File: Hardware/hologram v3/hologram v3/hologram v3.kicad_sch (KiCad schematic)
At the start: 700 parts, among them J1 USB_C_Receptacle_USB2.0_16P, J2 Conn_01x06_Socket, SW1 SW_Reset, SW2 SW_Boot, SW3 SW_opt1, SW4 SW_opt2, U1 SM16106SC, U10 SM16106SC, U11 SM16106SC, U12 SM16106SC, U13 SM16106SC, U14 SM16106SC, U15 SM16106SC, U16 SM16106SC, U17 SM16106SC, U18 SM16106SC, U19 SM16106SC, U2 SM16106SC, U20 SM16106SC, U21 SM16106SC, U22 SM16106SC, U23 SM16106SC, U24 SM16106SC, U25 SM16106SC, U26 SM16106SC, U27 SM16106SC, U28 SM16106SC, U29 SM16106SC, U3 SM16106SC, U30 SM16106SC, U31 SM16106SC, U32 SM16106SC, U33 ESP32-S3-WROOM-1(N16R8), U34 SY8286ARAC 12v->4v, U36 SY8286ARAC 12v->3.3v, U4 SM16106SC, U5 SM16106SC, U6 SM16106SC, U7 SM16106SC, U8 SM16106SC, U9 SM16106SC

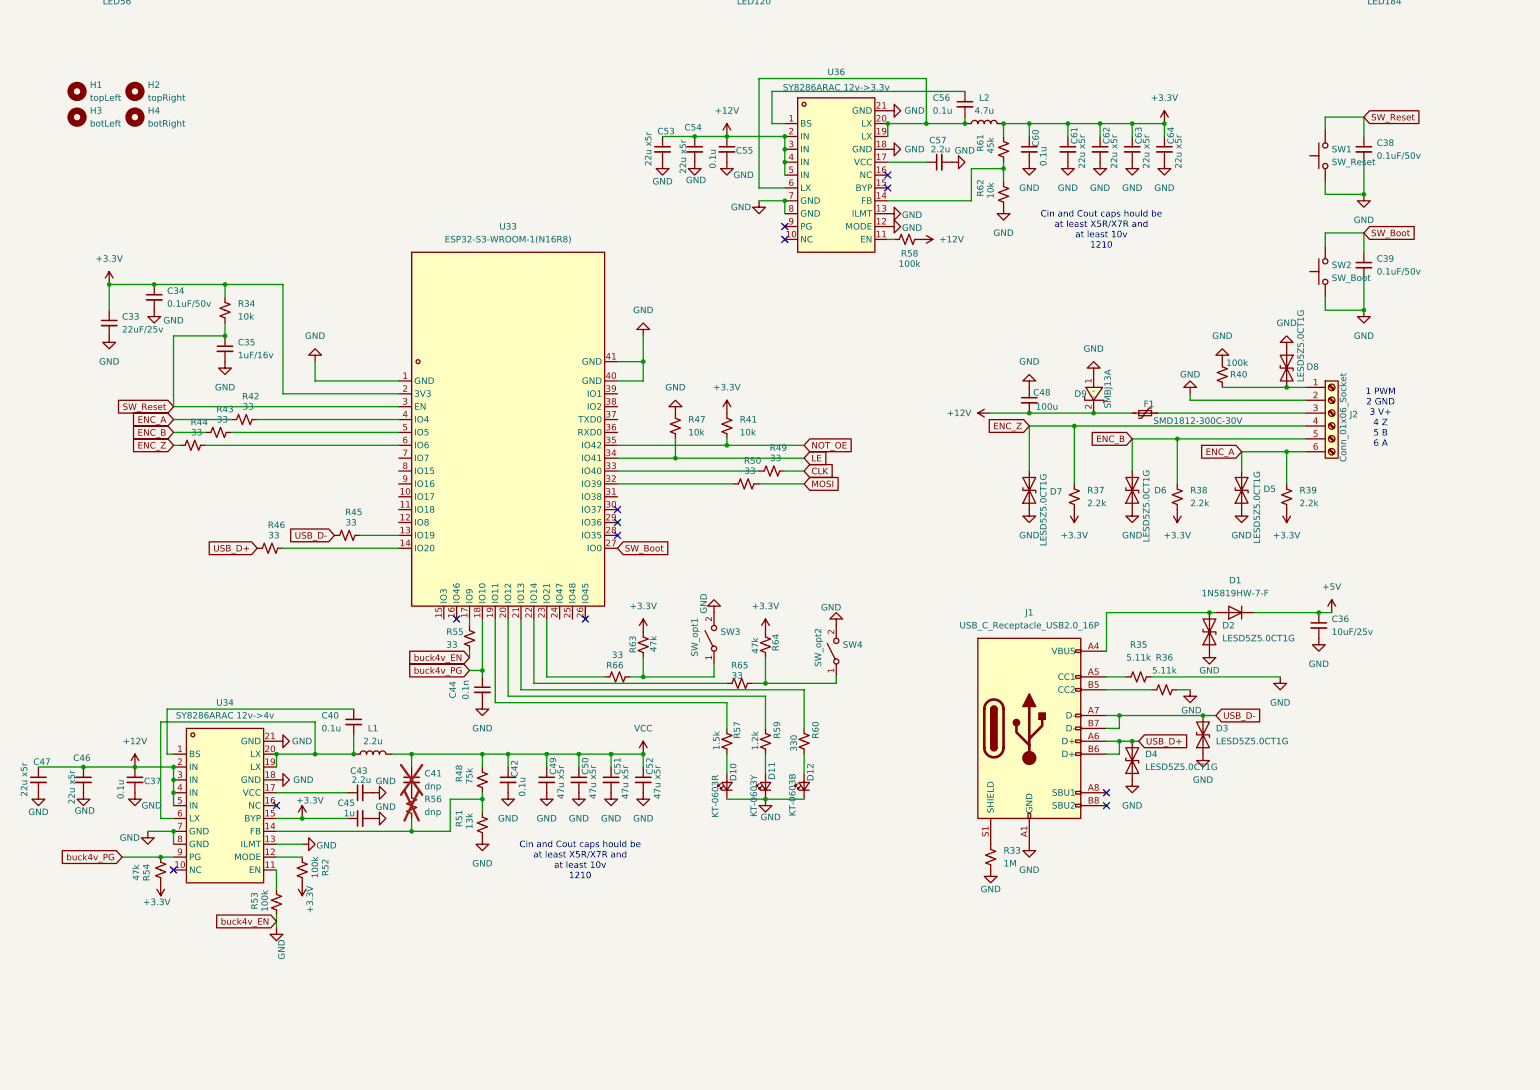
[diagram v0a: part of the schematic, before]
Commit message: kicad placed all parts, just need to wire 3.3v buck then review design
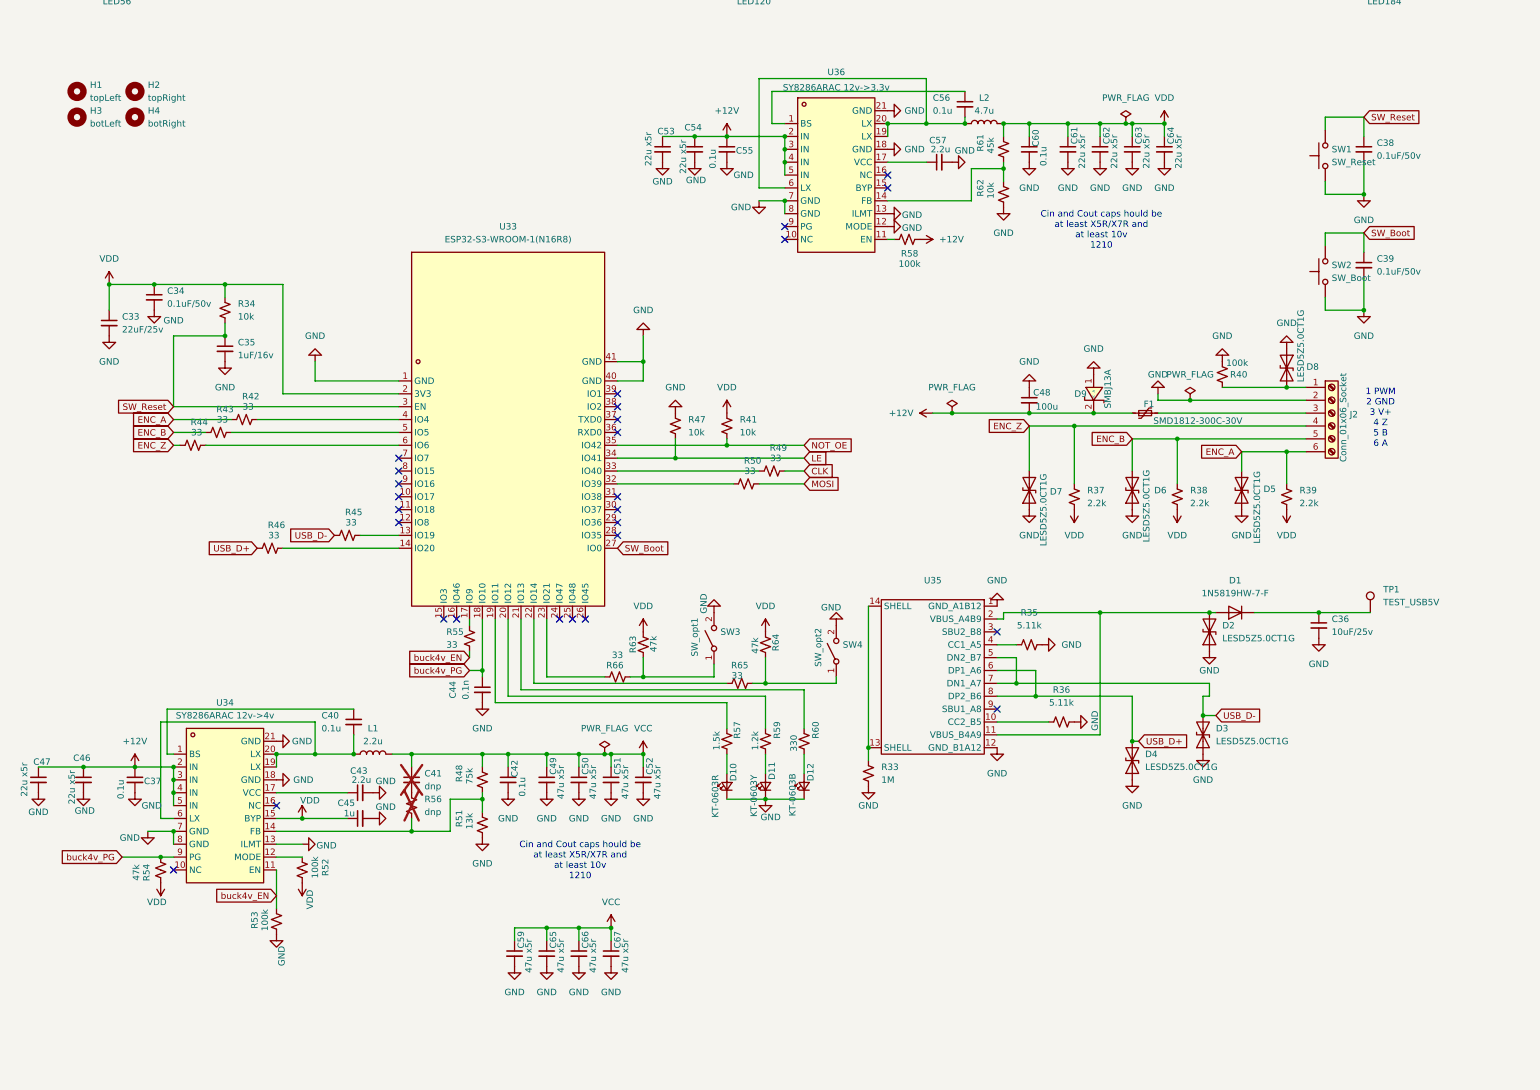
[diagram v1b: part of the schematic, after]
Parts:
- removed J1: USB_C_Receptacle_USB2.0_16P, easyeda:USB-C-SMD_TYPE-C-6PIN-2MD-073, symbol Connector:USB_C_Receptacle_USB2.0_16P
- added C59, C65, C66, C67: 47u x5r, Capacitor_SMD:C_1210_3225Metric, symbol Device:C_Small
- added TP1: TEST_USB5V, TestPoint:TestPoint_Pad_3.0x3.0mm, symbol Connector:TestPoint
- added U35: ~, easyeda:USB-C-SMD_TYPE-C-6PIN-2MD-073, symbol easyeda:Type-c_16pin_2md(073)
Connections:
- net +3.3V is gone; now on net VDD: C33.1, C34.1, C45.1, C60.1, C61.1, C62.1, C63.1, C64.1, L2.2, R34.1, R37.2, R38.2, R39.2, R41.1, R52.1, R54.1, R61.1, R63.2, R64.1, U33.2 (3V3), U34.15 (BYP)
- net GND: now also C59.2, C65.2, C66.2, C67.2, U35.1 (GND_A1B12), U35.12 (GND_B1A12); no longer R55.2
- net USB_D+: now also U35.6 (DP1_A6), U35.8 (DP2_B6)
- net USB_D-: now also U35.5 (DN2_B7), U35.7 (DN1_A7)
- net VCC: now also C59.1, C65.1, C66.1, C67.1
- net at R35.1: now also U35.4 (CC1_A5)
- net at D1.2 (A), D2.2 (A2): now also U35.11 (VBUS_B4A9), U35.2 (VBUS_A4B9)
- net at R36.1: now also U35.10 (CC2_B5)
- net at R33.1: now also U35.13 (SHELL), U35.14 (SHELL)
- net buck4v_EN: now reaches R53.1, U34.11 (EN)
- net buck4v_EN: now also R55.2
- net +5V: no longer names the net of C36.1, D1.1 (K)
- net +5V: now also TP1.1
- no-connect marks 14 -> 28
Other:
- moved on the sheet: R33, R35, R36, R53

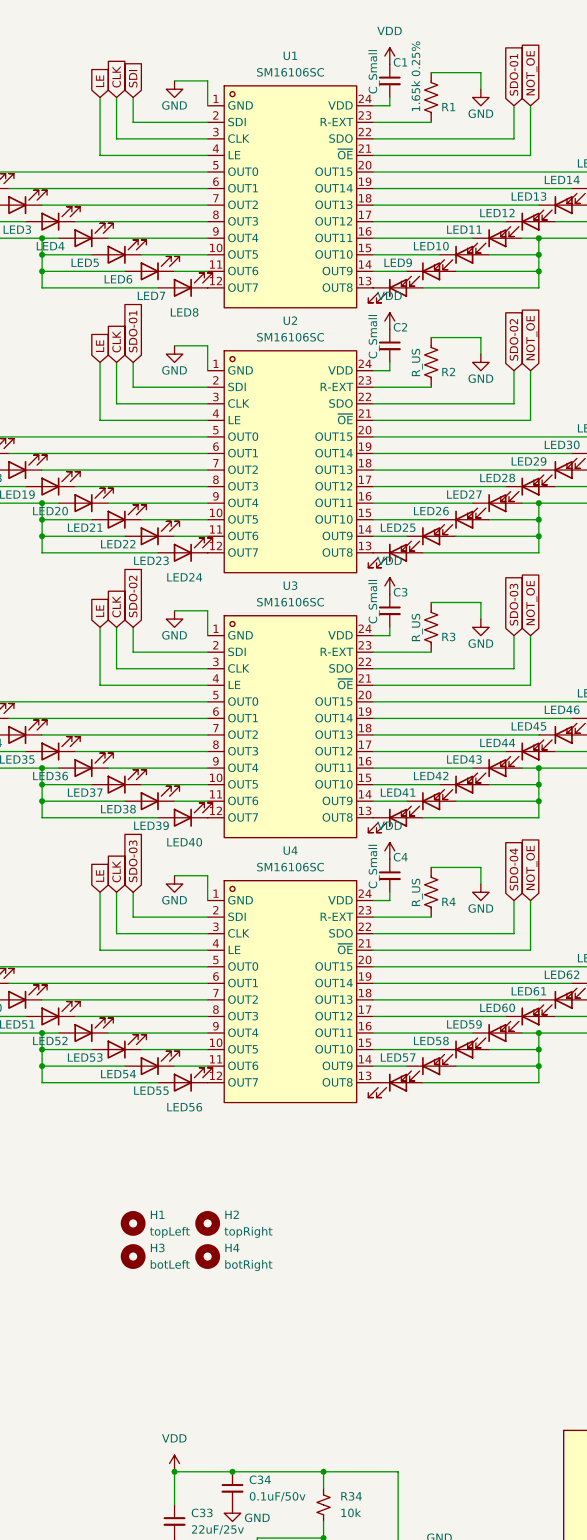
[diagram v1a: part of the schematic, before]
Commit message: kicad routed le, oe, clk, mosi, addded debug header pins
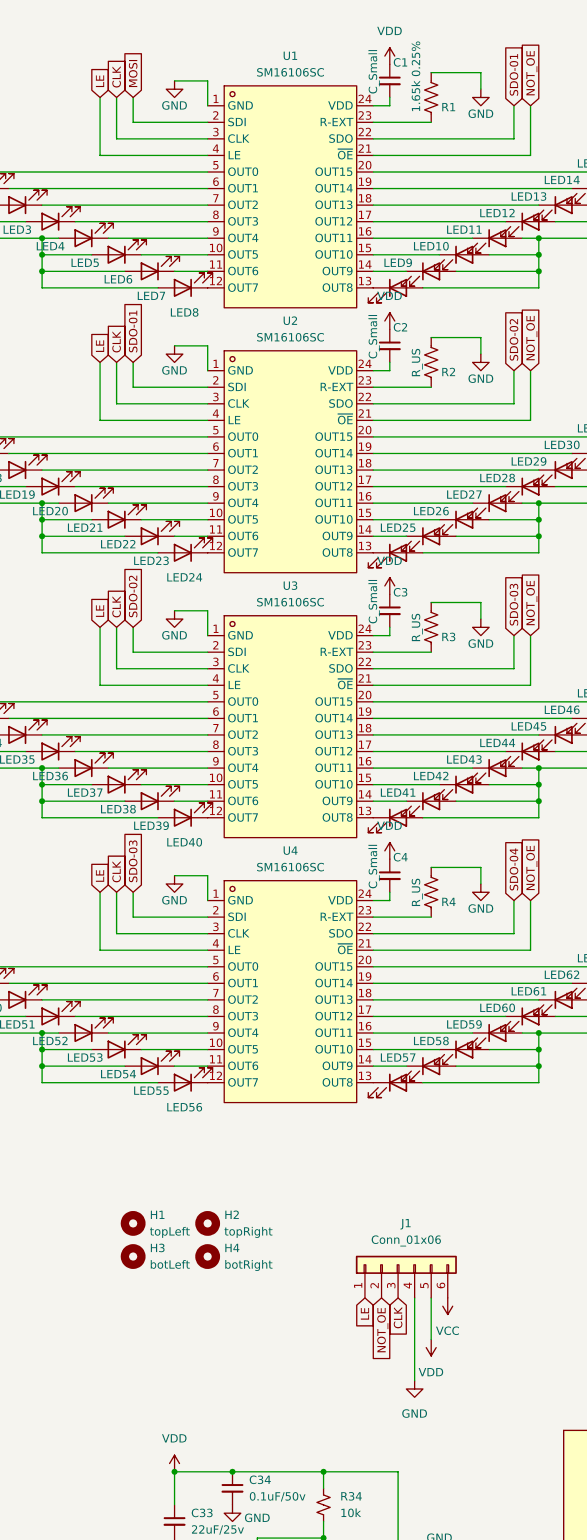
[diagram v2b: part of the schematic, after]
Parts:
- added J1: Conn_01x06, Connector_PinHeader_2.54mm:PinHeader_1x06_P2.54mm_Vertical, symbol Connector_Generic:Conn_01x06
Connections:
- net SDI is gone; now on net MOSI: U1.2 (SDI)
- net CLK: now also J1.3 (Pin_3)
- net GND: now also J1.4 (Pin_4)
- net LE: now also J1.1 (Pin_1)
- net NOT_OE: now also J1.2 (Pin_2)
- net VCC: now also J1.6 (Pin_6)
- net VDD: now also J1.5 (Pin_5)

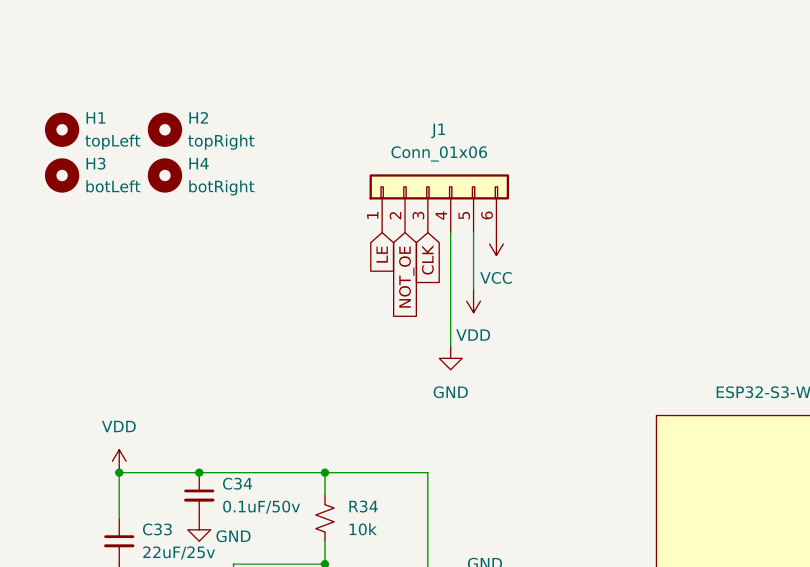
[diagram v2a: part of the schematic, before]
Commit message: wired in the debug pins
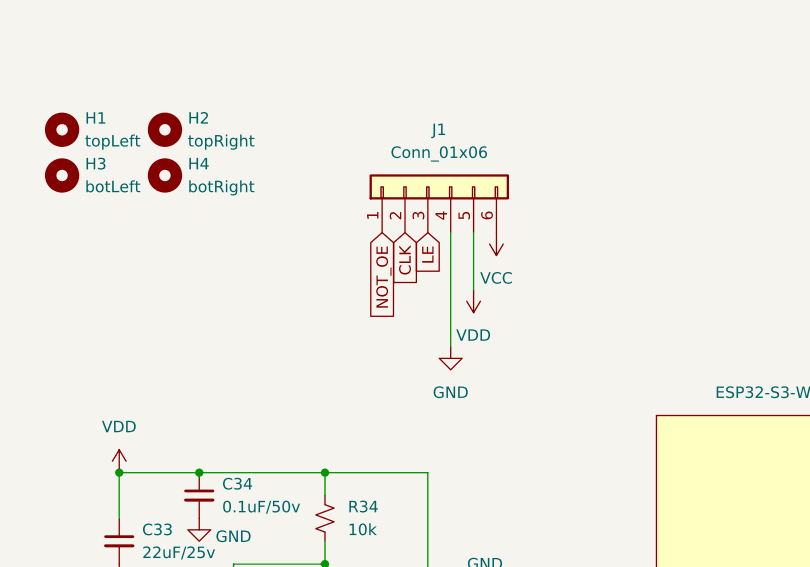
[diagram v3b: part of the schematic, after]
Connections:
- net CLK: now also J1.2 (Pin_2); no longer J1.3 (Pin_3)
- net LE: now also J1.3 (Pin_3); no longer J1.1 (Pin_1)
- net NOT_OE: now also J1.1 (Pin_1); no longer J1.2 (Pin_2)
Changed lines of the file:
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@@
 		)
 	)
-	(global_label "CLK"
-		(shape input)
-		(at 54.61 25.4 270)
-		(fields_autoplaced yes)
-		(effects
-			(font
-				(size 1.27 1.27)
-			)
-			(justify right)
-		)
-		(property "Intersheetrefs" "${INTERSHEET_REFS}"
-			(at 54.61 31.9533 90)
-			(effects
-				(font
-					(size 1.27 1.27)
-				)
-				(justify right)
-				(hide yes)
-			)
-		)
-	)
 	(global_label "buck4v_PG"
 		(shape input)
@@
 		)
 	)
-	(global_label "NOT_OE"
-		(shape input)
-		(at 52.07 25.4 270)
-		(fields_autoplaced yes)
-		(effects
-			(font
-				(size 1.27 1.27)
-			)
-			(justify right)
-		)
-		(property "Intersheetrefs" "${INTERSHEET_REFS}"
-			(at 52.07 35.4609 90)
-			(effects
-				(font
-					(size 1.27 1.27)
-				)
-				(justify right)
-				(hide yes)
-			)
-		)
-	)
 	(global_label "CLK"
 		(shape input)
@@
 		)
 	)
+	(global_label "NOT_OE"
+		(shape input)
+		(at 49.53 25.4 270)
+		(fields_autoplaced yes)
+		(effects
+			(font
+				(size 1.27 1.27)
+			)
+			(justify right)
+		)
+		(property "Intersheetrefs" "${INTERSHEET_REFS}"
+			(at 49.53 35.4609 90)
+			(effects
+				(font
+					(size 1.27 1.27)
+				)
+				(justify right)
+				(hide yes)
+			)
+		)
+	)
 	(global_label "SDO-12"
 		(shape input)
@@
 		)
 	)
+	(global_label "LE"
+		(shape input)
+		(at 54.61 25.4 270)
+		(fields_autoplaced yes)
+		(effects
+			(font
+				(size 1.27 1.27)
+			)
+			(justify right)
+		)
+		(property "Intersheetrefs" "${INTERSHEET_REFS}"
+			(at 54.61 30.5623 90)
+			(effects
+				(font
+					(size 1.27 1.27)
+				)
+				(justify right)
+				(hide yes)
+			)
+		)
+	)
 	(global_label "CLK"
 		(shape input)
@@
 	(global_label "CLK"
 		(shape input)
+		(at 52.07 25.4 270)
+		(fields_autoplaced yes)
+		(effects
+			(font
+				(size 1.27 1.27)
+			)
+			(justify right)
+		)
+		(property "Intersheetrefs" "${INTERSHEET_REFS}"
+			(at 52.07 31.9533 90)
+			(effects
+				(font
+					(size 1.27 1.27)
+				)
+				(justify right)
+				(hide yes)
+			)
+		)
+	)
+	(global_label "CLK"
+		(shape input)
 		(at 157.48 88.9 0)
 		(fields_autoplaced yes)
@@
 				(hide yes)
 			)
-		)
-	)
-	(global_label "LE"
-		(shape input)
-		(at 49.53 25.4 270)
-		(fields_autoplaced yes)
-		(effects
-			(font
-				(size 1.27 1.27)
-			)
-			(justify right)
-		)
-		(property "Intersheetrefs" "${INTERSHEET_REFS}"
-			(at 49.53 30.5623 90)
-			(effects
-				(font
-					(size 1.27 1.27)
-				)
-				(justify right)
-				(hide yes)
-			)

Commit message: hologram done and submitted for printing
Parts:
- C33: value 22uF/25v -> 22u
- C34, C38, C39: value 0.1uF/50v -> 0.1u
- C35: value 1uF/16v -> 1u
- C36: value 10uF/25v -> 10u
- C44: value 0.1n -> 0.1u
- C46, C47, C53, C54, C61, C62, C63, C64: value 22u x5r -> 22u
- C48: symbol Device:C_Small -> Device:C_Polarized_US; LCSC Part (none) -> C46550465
- C49, C50, C51, C52, C59, C65, C66, C67: value 47u x5r -> 47u
- D5, D6, D7, D8: symbol Device:D_TVS -> easyeda:LESD5Z5.0CT1G; LCSC Part (none) -> C136167
- D9: LCSC Part C10209 -> C151252
- F1: LCSC Part (none) -> C47002391
- J2: footprint TerminalBlock:TerminalBlock_MaiXu_MX126-5.0-06P_1x06_P5.00mm -> easyeda:CONN-TH_6P-P5.00_MX128-5.0-06P-GN01-CU-Y-A
- SW3: value SW_opt1 -> SW_OPT1
- SW4: value SW_opt2 -> SW_OPT2
- U35: LCSC Part (none) -> C2765186
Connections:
- net +12V: now also C48.1; no longer C48.2
- net GND: now also C48.2; no longer C48.1
